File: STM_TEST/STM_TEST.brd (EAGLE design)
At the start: 58.4 x 64.8 mm, 49 parts, among them U1 TPS2115APWR, U2 AZ1117EH-3.3TRG1, Y1 ECS-80-S-4X, Y2 ECS-80-S-4X

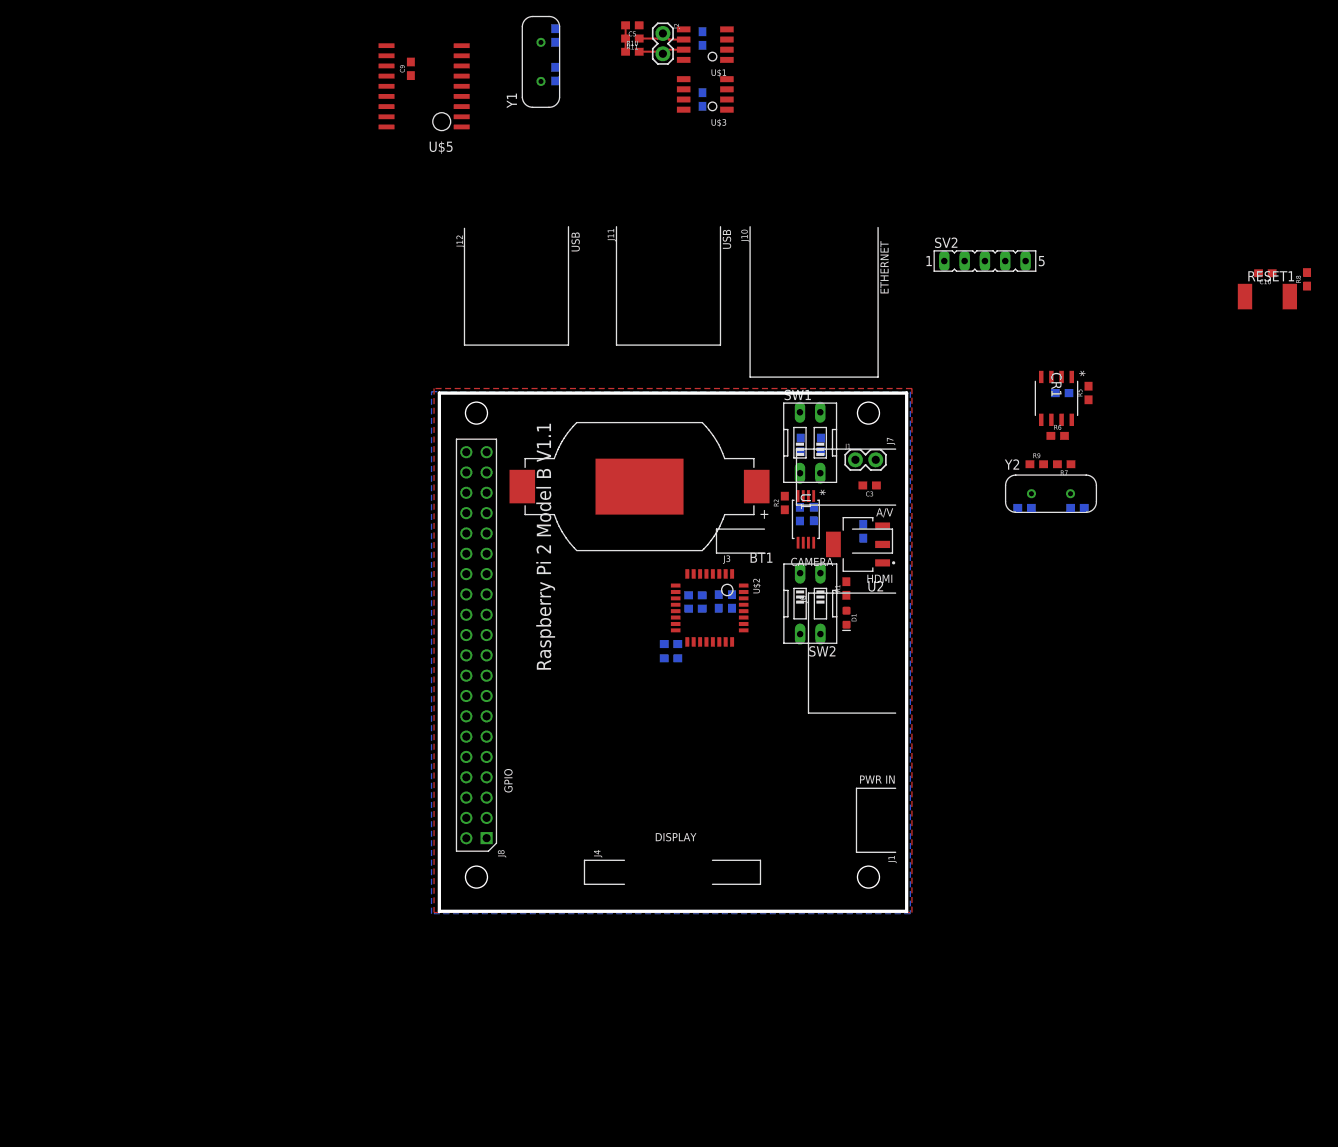
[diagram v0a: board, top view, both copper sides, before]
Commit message: Rerouting
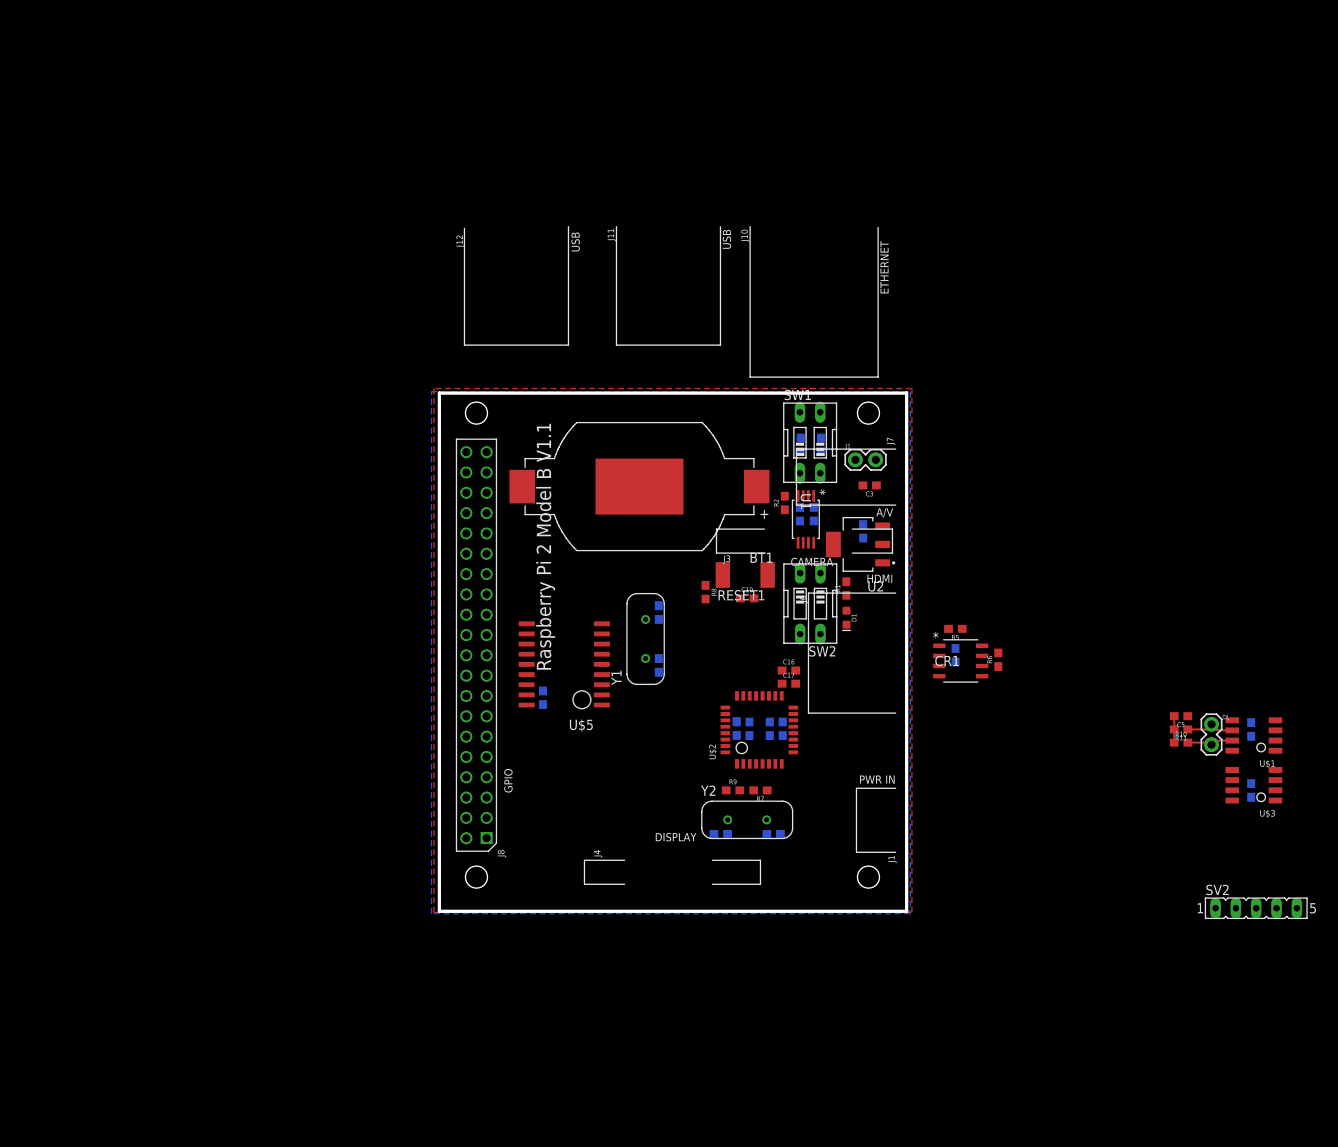
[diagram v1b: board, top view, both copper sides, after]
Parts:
- moved C5 110.3 mm to (145.3, 51.6)
- moved J2 110.3 mm to (149.1, 50.5)
- moved R10 110.3 mm to (145.3, 48.3)
- moved C6 110.3 mm to (154.1, 42.3)
- moved R11 110.3 mm to (145.3, 49.9)
- moved C7 110.3 mm to (154.1, 49.9)
- moved U$1 110.3 mm to (157.1, 51.1)
- moved U$3 110.3 mm to (157.1, 44.8)
- moved SV2 87.7 mm to (154.7, 27.6)
- moved R8 84.8 mm to (85.9, 67.1), turned to 270 degrees
- moved C9 80.3 mm to (65.5, 53.9), flipped to the bottom
- moved C10 76.5 mm to (91.1, 66.3), turned to 0 degrees
- moved C11 75.0 mm to (80.0, 57.9), turned to 270 degrees
- moved U$5 74.4 mm to (72.9, 63.1)
- moved RESET1 74.0 mm to (90.8, 69.2), turned to 180 degrees
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
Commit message: routing
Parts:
- removed C3, C4: 1.0uF, SparkFun-Capacitors:0603
- removed SW1: (no value), special:EDG-02
- removed U2: AZ1117EH-3.3TRG1, AZ1117EH-3.3TRG1:SOT230P700X180-4N
- added R12, R13, R14: 10k, SparkFun-Resistors:0603
- moved U$3 89.6 mm to (67.6, 47.2), turned to 0 degrees
- moved C6 89.2 mm to (65.0, 47.6), flipped to the top
- moved U$1 74.8 mm to (82.3, 49.7), turned to 270 degrees
- moved C7 70.6 mm to (83.6, 46.1), turned to 0 degrees
- moved J2 66.9 mm to (82.8, 41.7), turned to 0 degrees
- moved C5 65.4 mm to (81.9, 35.4), turned to 270 degrees
- moved R11 63.4 mm to (83.6, 35.4), turned to 270 degrees
- moved R10 61.4 mm to (85.2, 35.4), turned to 90 degrees
- moved SV2 61.2 mm to (95.6, 43.6)
- moved R6 29.9 mm to (92.8, 62.4), flipped to the bottom
- moved C19 24.4 mm to (109.1, 48.8), turned to 270 degrees
- moved CR1 24.4 mm to (93.7, 63.0)
- moved C20 23.7 mm to (109.1, 55.4), turned to 90 degrees
- moved Y2 21.1 mm to (107.3, 52.1), turned to 90 degrees
- moved R5 19.6 mm to (98.0, 66.9)
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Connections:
- removed net D1: R3.2, SW1.1, U1.3
- removed net SCL: PCB1.P$5
- removed net SDA: PCB1.P$3
- removed net VCC: C3.1, J1.2, U2.3
- new net +3V3ROV_ADC2: R3.1, R4.2, U$2.PA2
- new net +5V_ADC1: R13.1, R14.2, U$2.PA1
- net +3V3ROV: now also J1.2, R12.2, R3.2; no longer C4.1, R3.1, R4.1, U2.2, U2.4
- net +5V: now also R13.2
- net D0: now also R12.1; no longer R4.2, SW1.2
- net GND: now also R14.1, R4.1, U1.3; no longer C3.2, C4.2, SW1.3, SW1.4, U2.1
- net I2C1_SCL: now also PCB1.P$5
- net I2C1_SDA: now also PCB1.P$3
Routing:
- net +3V3: track 0.00 -> 176.5 mm, vias 0 -> 2
- net I2C1_SDA: track 0.00 -> 39.1 mm, vias 0 -> 2
- net I2C1_SCL: track 0.00 -> 38.4 mm, vias 0 -> 2
- net +5V_ADC1: track 0.00 -> 34.6 mm, vias 0 -> 1
- net NRST: track 0.00 -> 32.4 mm, vias 0 -> 3
- net CAN_H: track 5.88 -> 31.2 mm, vias 0 -> 1
- net CAN_L: track 6.18 -> 30.8 mm
- net +3V3ROV: track 0.00 -> 24.1 mm, vias 0 -> 1
- net NSS: track 0.00 -> 24.0 mm, vias 0 -> 2
- net +3V3ROV_ADC2: track 0.00 -> 21.7 mm, vias 0 -> 1
- net +5V: track 0.00 -> 21.5 mm
- net CE0: track 0.00 -> 15.1 mm
- net SWDIO: track 0.00 -> 15.0 mm, vias 0 -> 1
- net SWCLK: track 0.00 -> 12.9 mm, vias 0 -> 1
- net SCK: track 0.00 -> 12.4 mm, vias 0 -> 1
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- added copper zone on layer 1, net +3V3

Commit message: uhhh, yeah boards looking good
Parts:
- added C3: 0.1uF, SparkFun-Capacitors:0603
- added U$4: ACS711, ACS711_ameter:ACS711
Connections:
- new net +5V_TO_PI: U$4.IP1-, U$4.IP2-
- new net PI_CURRENT: U$2.PA0, U$4.VIOUT
- net +3V3: now also C3.1, U$4.VCC
- net +5V: now also U$4.IP1+, U$4.IP2+
- net GND: now also C3.2, U$4.GND
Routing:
- net PI_CURRENT: track 0.00 -> 42.9 mm, vias 0 -> 2
- net +3V3: track 176.5 -> 217.7 mm
- net +5V: track 21.5 -> 22.9 mm, vias 0 -> 1
- net +5V_TO_PI: track 0.00 -> 1.27 mm
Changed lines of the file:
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@@
 <attribute name="PROD_ID" value="RES-07856" x="76.073" y="39.878" size="1.778" layer="28" rot="MR180" display="off"/>
+</element>
+<element name="U$4" library="ACS711_ameter" package="ACS711" value="ACS711" x="69.342" y="33.02"/>
+<element name="C3" library="SparkFun-Capacitors" library_urn="urn:adsk.eagle:library:510" package="0603" package3d_urn="urn:adsk.eagle:package:37414/1" value="0.1uF" x="74.295" y="35.941" rot="R90">
+<attribute name="PROD_ID" value="CAP-08280" x="74.295" y="35.941" size="1.778" layer="27" rot="R90" display="off"/>
 </element>
 </elements>
@@
 <contactref element="R4" pad="1"/>
 <contactref element="R14" pad="1"/>
-<wire x1="75.223" y1="39.878" x2="101.854" y2="74.51" width="0" layer="19" extent="1-1"/>
-<wire x1="108.845" y1="63.627" x2="75.223" y2="39.878" width="0" layer="19" extent="1-1"/>
+<contactref element="C3" pad="2"/>
+<contactref element="U$4" pad="GND"/>
 <wire x1="91.0673" y1="61.138" x2="92.824" y2="63.28" width="0" layer="19" extent="1-16"/>
+<wire x1="90.74" y1="57.838" x2="91.0673" y2="61.138" width="0" layer="19" extent="1-1"/>
 </signal>
 <signal name="+3V3BAT">
@@
 <via x="83.566" y="47.625" extent="1-16" drill="0.35"/>
 <wire x1="83.566" y1="47.625" x2="83.566" y2="49.657" width="0.254" layer="1"/>
+<contactref element="U$4" pad="VCC"/>
+<contactref element="C3" pad="1"/>
+<wire x1="100.711" y1="43.561" x2="100.711" y2="36.449" width="0.254" layer="1"/>
+<wire x1="100.711" y1="36.449" x2="97.028" y2="32.766" width="0.254" layer="1"/>
+<wire x1="97.028" y1="32.766" x2="81.28" y2="32.766" width="0.254" layer="1"/>
+<wire x1="81.28" y1="32.766" x2="80.01" y2="34.036" width="0.254" layer="1"/>
+<wire x1="80.01" y1="34.036" x2="80.01" y2="36.322" width="0.254" layer="1"/>
+<wire x1="80.01" y1="36.322" x2="79.375" y2="36.957" width="0.254" layer="1"/>
+<wire x1="79.375" y1="36.957" x2="77.724" y2="36.957" width="0.254" layer="1"/>
+<wire x1="77.724" y1="36.957" x2="75.819" y2="35.052" width="0.254" layer="1"/>
+<wire x1="75.819" y1="35.052" x2="74.334" y2="35.052" width="0.254" layer="1"/>
+<wire x1="74.334" y1="35.052" x2="74.295" y2="35.091" width="0.254" layer="1"/>
+<wire x1="72.14199375" y1="34.925" x2="74.207" y2="34.925" width="0.254" layer="1"/>
+<wire x1="74.207" y1="34.925" x2="74.334" y2="35.052" width="0.254" layer="1"/>
 </signal>
 <signal name="NRST">
@@
 </signal>
 <signal name="+5V">
+<contactref element="R13" pad="2"/>
+<contactref element="PCB1" pad="P$2"/>
+<contactref element="U$4" pad="IP1+"/>
+<contactref element="U$4" pad="IP2+"/>
+<wire x1="75.223" y1="41.656" x2="73.533" y2="41.656" width="0.254" layer="16"/>
+<wire x1="73.533" y1="41.656" x2="73.406" y2="41.529" width="0.254" layer="16"/>
+<via x="73.406" y="41.529" extent="1-16" drill="0.35"/>
+<wire x1="73.406" y1="41.529" x2="69.469" y2="37.592" width="0.254" layer="1"/>
+<wire x1="69.469" y1="37.592" x2="57.023" y2="37.592" width="0.254" layer="1"/>
+<wire x1="57.023" y1="37.592" x2="55.9452" y2="36.5142" width="0.254" layer="1"/>
+<wire x1="55.9452" y1="36.5142" x2="55.9452" y2="36.3076" width="0.254" layer="1"/>
+<wire x1="66.54200625" y1="34.925" x2="66.54200625" y2="33.655" width="0.3048" layer="1"/>
 <contactref element="PCB1" pad="P$4"/>
-<contactref element="PCB1" pad="P$2"/>
-<contactref element="R13" pad="2"/>
-<wire x1="55.9452" y1="36.3076" x2="57.3566" y2="37.719" width="0.254" layer="16"/>
-<wire x1="68.961" y1="37.719" x2="72.898" y2="41.656" width="0.254" layer="16"/>
-<wire x1="72.898" y1="41.656" x2="75.223" y2="41.656" width="0.254" layer="16"/>
-<wire x1="57.3566" y1="37.719" x2="68.961" y2="37.719" width="0.254" layer="16"/>
-<wire x1="57.3566" y1="37.719" x2="55.9452" y2="38.8476" width="0" layer="19" extent="16-16"/>
+<wire x1="69.469" y1="37.592" x2="66.54200625" y2="34.925" width="0" layer="19" extent="1-1"/>
+<wire x1="55.9452" y1="38.8476" x2="57.023" y2="37.592" width="0" layer="19" extent="1-1"/>
 </signal>
 <signal name="RESET">
@@
 <wire x1="76.923" y1="45.681" x2="77.724" y2="46.482" width="0.254" layer="16"/>
 <wire x1="77.724" y1="46.482" x2="77.724" y2="50.673" width="0.254" layer="16"/>
-<wire x1="77.724" y1="50.673" x2="80.137" y2="53.086" width="0.254" layer="16"/>
+<wire x1="77.724" y1="50.673" x2="78.613" y2="51.562" width="0.254" layer="16"/>
+<wire x1="78.613" y1="51.562" x2="80.137" y2="53.086" width="0.254" layer="16"/>
 <wire x1="80.137" y1="53.086" x2="81.788" y2="53.086" width="0.254" layer="16"/>
 <wire x1="81.788" y1="53.086" x2="82.169" y2="53.467" width="0.254" layer="16"/>
@@
 <wire x1="96.901" y1="57.531" x2="96.901" y2="56.515" width="0.254" layer="1"/>
 </signal>
+<signal name="PI_CURRENT">
+<contactref element="U$2" pad="PA0"/>
+<contactref element="U$4" pad="VIOUT"/>
+<wire x1="72.14199375" y1="33.655" x2="76.581" y2="33.655" width="0.254" layer="1"/>
+<wire x1="76.581" y1="33.655" x2="78.613" y2="35.687" width="0.254" layer="1"/>
+<via x="78.613" y="35.687" extent="1-16" drill="0.35"/>
+<wire x1="78.613" y1="35.687" x2="78.613" y2="47.752" width="0.254" layer="16"/>
+<wire x1="78.613" y1="47.752" x2="79.248" y2="48.387" width="0.254" layer="16"/>
+<wire x1="79.248" y1="48.387" x2="79.248" y2="50.8" width="0.254" layer="16"/>
+<wire x1="79.248" y1="50.8" x2="80.899" y2="52.451" width="0.254" layer="16"/>
+<wire x1="80.899" y1="52.451" x2="81.915" y2="52.451" width="0.254" layer="16"/>
+<wire x1="81.915" y1="52.451" x2="82.804" y2="53.34" width="0.254" layer="16"/>
+<wire x1="82.804" y1="53.34" x2="94.488" y2="53.34" width="0.254" layer="16"/>
+<wire x1="94.488" y1="53.34" x2="95.885" y2="54.737" width="0.254" layer="16"/>
+<via x="95.885" y="54.737" extent="1-16" drill="0.35"/>
+<wire x1="95.885" y1="54.737" x2="95.936" y2="54.788" width="0.254" layer="1"/>
+<wire x1="95.936" y1="54.788" x2="97.79" y2="54.788" width="0.254" layer="1"/>
+</signal>
+<signal name="+5V_TO_PI">
+<contactref element="U$4" pad="IP1-"/>
+<contactref element="U$4" pad="IP2-"/>
+<wire x1="66.54200625" y1="32.385" x2="66.54200625" y2="31.115" width="0.3048" layer="1"/>
+</signal>
 </signals>

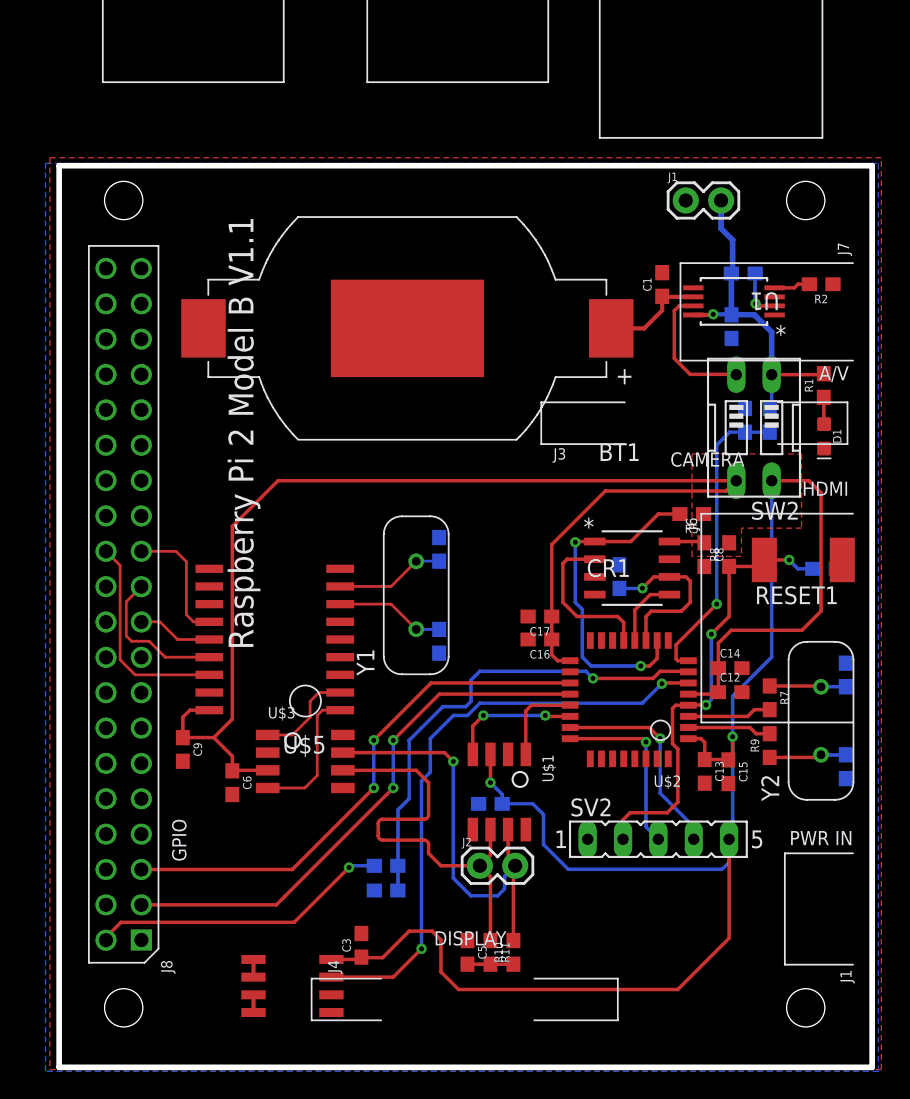
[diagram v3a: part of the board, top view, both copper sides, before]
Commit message: Routing Complete
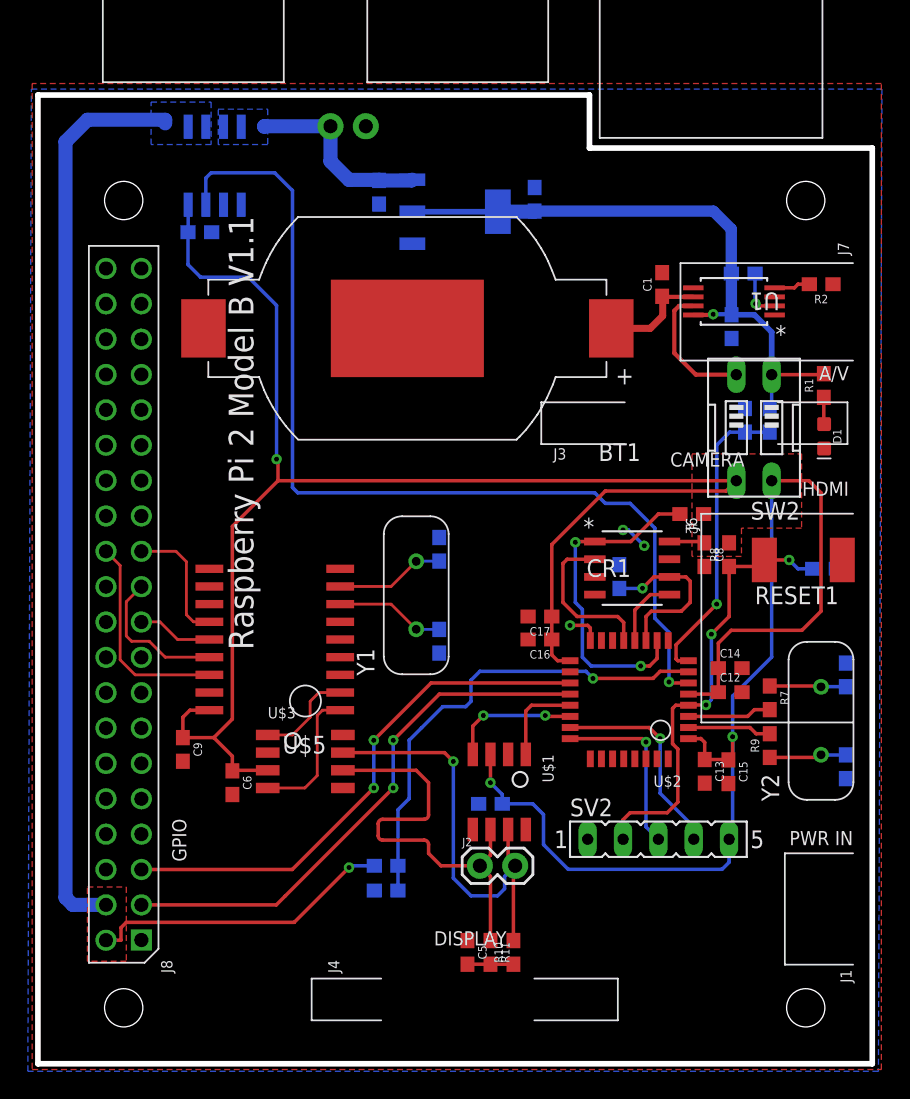
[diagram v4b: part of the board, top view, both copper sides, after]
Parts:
- added C21, C4: 1.0uF, SparkFun-Capacitors:0603
- added U2: AZ1117EH-3.3TRG1, AZ1117EH-3.3TRG1:SOT230P700X180-4N
- moved U$4 59.2 mm to (63.8, 91.9), flipped to the bottom, turned to 270 degrees
- moved C3 52.5 mm to (62.7, 87.2), flipped to the bottom, turned to 180 degrees
- moved J1 23.6 mm to (74.6, 94.8), flipped to the bottom
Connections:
- removed net +5V_TO_PI: U$4.IP1-, U$4.IP2-
- new net VCC: C4.1, J1.2, U$4.IP1-, U$4.IP2-, U2.3
- net +3V3ROV: now also C21.1, U2.2, U2.4; no longer J1.2
- net GND: now also C21.2, C4.2, U2.1
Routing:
- net +5V: track 22.9 -> 87.5 mm
- net PI_CURRENT: track 42.9 -> 70.3 mm, vias 2 -> 1
- net +3V3ROV: track 24.1 -> 45.2 mm
- net +3V3: track 217.7 -> 201.1 mm, vias 2 -> 3
- net VCC: track 0.00 -> 13.9 mm
- net GND: track 0.00 -> 4.44 mm, vias 0 -> 3
- net +5V_TO_PI: track 1.27 -> 0.00 mm
- added copper zone on layer 1, net +5V
- added copper zone on layer 16, net +5V
- added copper zone on layer 16, net VCC
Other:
- board size 58.4 x 64.8 mm -> 59.9 x 69.6 mm
